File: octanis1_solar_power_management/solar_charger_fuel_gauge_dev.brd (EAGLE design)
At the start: 100 x 30 mm, 116 parts, among them IC1 REG1117, IC401 TUSB2046BIRHBIRHB, Q2 32.768kHz, Q4 CSTCR4M00G15L99, Q401 CSTCR6M00G15L99, T1 BC547, T2 BC547, U1 BQ24210, U2 BQ27510_DRZ_12, U3 DRV8836DSSR, U4 DRV8836DSSR, U402 TPS62237DRY, U404 TPD2E001DRLR, U5 DRV8836DSSR, U6 MSP430F5529IPNR, U7 DRV8836DSSR

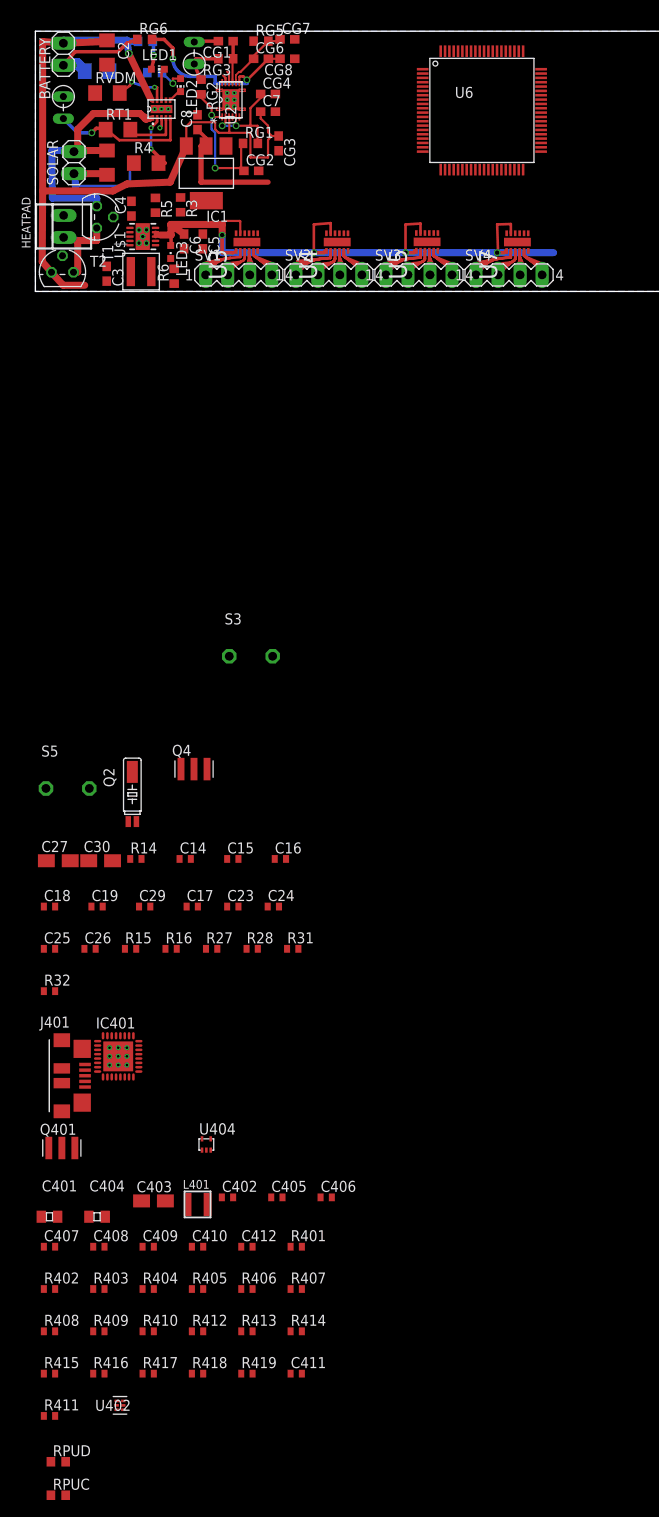
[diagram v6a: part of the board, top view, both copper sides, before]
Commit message: connected h-bridges to pins
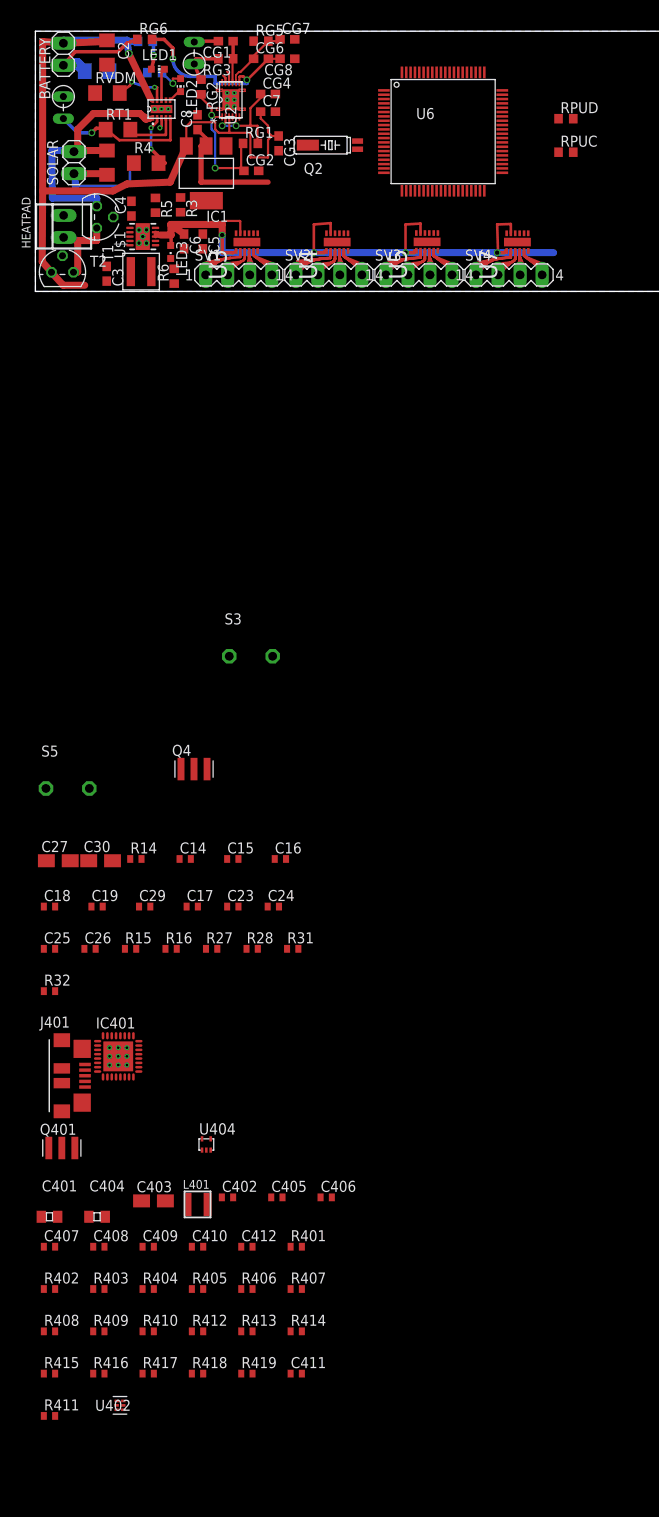
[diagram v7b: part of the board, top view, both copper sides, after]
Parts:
- moved RPUD 165.5 mm to (61.2, 19.9)
- moved RPUC 165.5 mm to (61.2, 16.1)
- moved Q2 76.6 mm to (32.7, 16.9), turned to 90 degrees
- moved U6 5.09 mm to (47.0, 18.4)

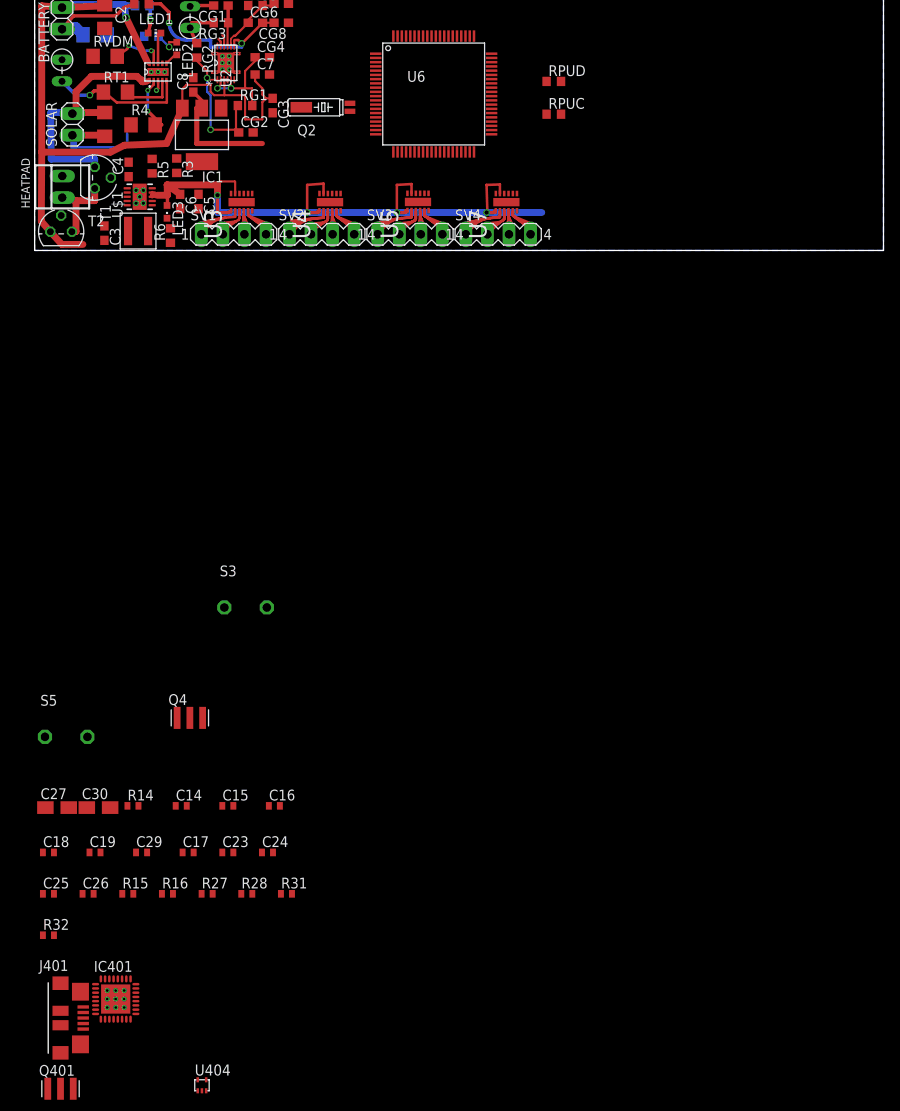
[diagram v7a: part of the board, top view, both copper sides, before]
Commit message: h-bridge: connected sleep pin with mode pin
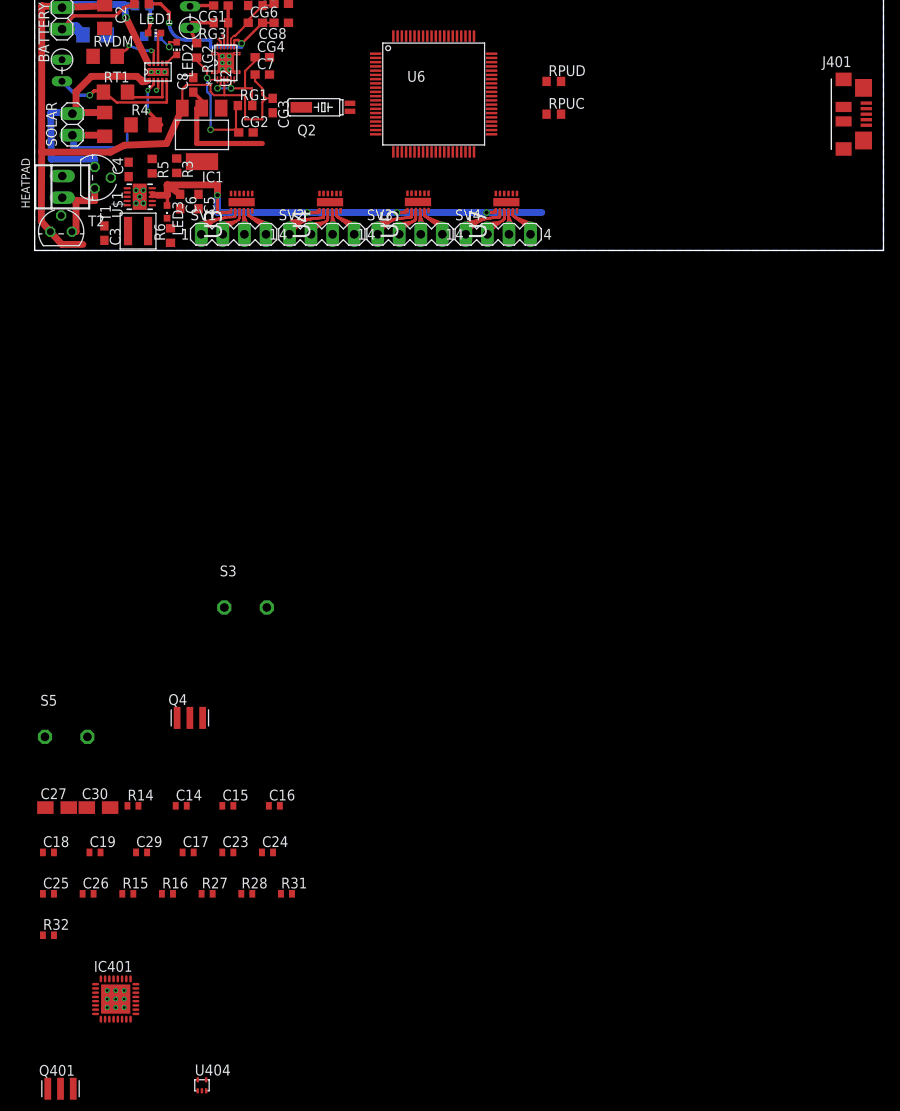
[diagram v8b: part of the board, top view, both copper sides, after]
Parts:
- moved J401 140.9 mm to (95.3, 16.1)
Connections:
- net +5V: no longer U3.11, U4.11, U5.11, U7.11
- net M12SLEEP: now also U3.11
- net M34SLEEP: now also U4.11
- net M56SLEEP: now also U5.11
- net M78SLEEP: now also U7.11
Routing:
- net +5V: track 84.1 -> 62.1 mm
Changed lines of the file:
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@@
 <attribute name="PACKAGE_DESIGNATOR" value="DRY" x="-3.8608" y="-84.328" size="1.778" layer="27" display="off"/>
 </element>
-<element name="J401" library="usb_con-update" package="HIROSE-ZX62R-B-5P" value="" x="3.048" y="-90.424"/>
+<element name="J401" library="usb_con-update" package="HIROSE-ZX62R-B-5P" value="" x="95.3008" y="16.0528"/>
 <element name="C404" library="CAP" package="CSMD0805" value="1u" x="7.112" y="-106.68"/>
 <element name="C401" library="CAP" package="CSMD0805" value="1u" x="1.6256" y="-106.68"/>
@@
 <wire x1="19.3444" y1="-124.7648" x2="25.034" y2="-124.7648" width="0" layer="19" extent="1-1"/>
 <wire x1="18.0444" y1="-119.888" x2="19.3444" y2="-124.7648" width="0" layer="19" extent="1-1"/>
-<wire x1="5.723" y1="-89.124" x2="3.048" y2="-98.7552" width="0" layer="19" extent="1-1"/>
-<wire x1="7.1754" y1="-89.4388" x2="5.723" y2="-89.124" width="0" layer="19" extent="1-1"/>
+<wire x1="97.9758" y1="17.3528" x2="3.048" y2="-98.7552" width="0" layer="19" extent="1-1"/>
+<wire x1="7.1754" y1="-89.4388" x2="97.9758" y2="17.3528" width="0" layer="19" extent="1-1"/>
 <wire x1="8.3004" y1="-85.8138" x2="7.1754" y2="-89.4388" width="0" layer="19" extent="1-1"/>
 <wire x1="9.8004" y1="-85.8138" x2="8.3004" y2="-85.8138" width="0" layer="19" extent="1-1"/>
@@
 <wire x1="21.5392" y1="6.5024" x2="21.5392" y2="4.4704" width="0.8128" layer="16"/>
 <wire x1="21.5392" y1="4.4704" x2="32.1056" y2="4.4704" width="0.8128" layer="16"/>
-<contactref element="U3" pad="11"/>
-<contactref element="U4" pad="11"/>
-<contactref element="U5" pad="11"/>
-<contactref element="U7" pad="11"/>
 <wire x1="32.1056" y1="4.4704" x2="42.672" y2="4.4704" width="0.8128" layer="16"/>
 <wire x1="42.672" y1="4.4704" x2="53.2384" y2="4.4704" width="0.8128" layer="16"/>
 <wire x1="53.2384" y1="4.4704" x2="59.7408" y2="4.4704" width="0.8128" layer="16"/>
-<wire x1="23.622" y1="6.7056" x2="23.622" y2="8.0772" width="0.254" layer="1"/>
-<wire x1="23.622" y1="8.0772" x2="23.5712" y2="8.128" width="0.254" layer="1"/>
-<wire x1="23.5712" y1="8.128" x2="21.9456" y2="8.128" width="0.254" layer="1"/>
-<wire x1="21.9456" y1="8.128" x2="21.5392" y2="7.7216" width="0.254" layer="1"/>
 <wire x1="23.1394" y1="4.6736" x2="22.8854" y2="4.4958" width="0.3048" layer="1"/>
 <wire x1="22.8854" y1="4.4958" x2="22.7584" y2="4.4704" width="0.4064" layer="1"/>
@@
 <wire x1="21.5392" y1="4.4704" x2="21.5392" y2="6.5024" width="0.4064" layer="1"/>
 <via x="32.1056" y="4.4704" extent="1-16" drill="0.5"/>
-<wire x1="34.036" y1="6.7056" x2="34.036" y2="7.874" width="0.3048" layer="1"/>
-<wire x1="34.036" y1="7.874" x2="32.1056" y2="7.7216" width="0.3048" layer="1"/>
-<wire x1="32.1056" y1="7.7216" x2="32.1056" y2="4.4704" width="0.3048" layer="1"/>
 <wire x1="43.9166" y1="4.699" x2="43.688" y2="4.699" width="0.3048" layer="1"/>
 <wire x1="43.688" y1="4.699" x2="43.688" y2="4.4704" width="0.3048" layer="1"/>
 <wire x1="43.688" y1="4.4704" x2="42.672" y2="4.4704" width="0.4064" layer="1"/>
 <via x="42.672" y="4.4704" extent="1-16" drill="0.5"/>
-<wire x1="44.3992" y1="6.731" x2="44.3992" y2="7.8232" width="0.3048" layer="1"/>
-<wire x1="44.3992" y1="7.8232" x2="42.672" y2="7.7216" width="0.3048" layer="1"/>
-<wire x1="42.672" y1="7.7216" x2="42.672" y2="4.4704" width="0.3048" layer="1"/>
 <wire x1="54.3306" y1="4.6736" x2="54.1528" y2="4.6736" width="0.3048" layer="1"/>
 <wire x1="54.1528" y1="4.6736" x2="54.1528" y2="4.4704" width="0.3048" layer="1"/>
-<wire x1="54.1528" y1="4.4704" x2="53.34" y2="4.4704" width="0.4064" layer="1"/>
+<wire x1="54.1528" y1="4.4704" x2="53.2384" y2="4.4704" width="0.4064" layer="1"/>
 <via x="53.2384" y="4.4704" extent="1-16" drill="0.5"/>
-<wire x1="53.34" y1="4.4704" x2="53.2384" y2="4.4704" width="0.4064" layer="1"/>
-<wire x1="54.8132" y1="6.7056" x2="54.8132" y2="7.7724" width="0.3048" layer="1"/>
-<wire x1="54.8132" y1="7.7724" x2="53.2384" y2="7.7216" width="0.3048" layer="1"/>
-<wire x1="53.2384" y1="7.7216" x2="53.34" y2="4.4704" width="0.3048" layer="1"/>
 <wire x1="33.5534" y1="4.6736" x2="33.3756" y2="4.6736" width="0.3048" layer="1"/>
 <wire x1="33.3756" y1="4.6736" x2="33.3756" y2="4.4704" width="0.3048" layer="1"/>
 <wire x1="33.3756" y1="4.4704" x2="32.1056" y2="4.4704" width="0.4064" layer="1"/>
-<wire x1="53.2384" y1="7.7216" x2="49.7578" y2="25.2552" width="0" layer="19" extent="1-1"/>
+<wire x1="54.1528" y1="4.6736" x2="49.7578" y2="25.2552" width="0" layer="19" extent="1-1"/>
 <wire x1="16.7386" y1="9.1322" x2="15.6092" y2="7.7216" width="0" layer="19" extent="1-1"/>
 <wire x1="19.304" y1="6.6158" x2="17.145" y2="6.6158" width="0" layer="19" extent="1-1"/>
@@
 <contactref element="J401" pad="SHIELD1"/>
 <contactref element="R401" pad="1"/>
-<wire x1="29.4236" y1="-110.1344" x2="3.048" y2="-86.324" width="0" layer="19" extent="1-1"/>
+<wire x1="29.4236" y1="-110.1344" x2="95.3008" y2="20.1528" width="0" layer="19" extent="1-1"/>
 </signal>
 <signal name="N$16">
@@
 <contactref element="R405" pad="2"/>
 <wire x1="19.2104" y1="-97.6988" x2="19.3444" y2="-115.0112" width="0" layer="19" extent="1-1"/>
-<wire x1="5.723" y1="-90.424" x2="19.2104" y2="-97.6988" width="0" layer="19" extent="1-1"/>
+<wire x1="97.9758" y1="16.0528" x2="19.2104" y2="-97.6988" width="0" layer="19" extent="1-1"/>
 </signal>
 <signal name="N$17">
@@
 <contactref element="R406" pad="2"/>
 <wire x1="20.2104" y1="-98.9988" x2="25.034" y2="-115.0112" width="0" layer="19" extent="1-1"/>
-<wire x1="5.723" y1="-91.074" x2="20.2104" y2="-98.9988" width="0" layer="19" extent="1-1"/>
+<wire x1="97.9758" y1="15.4028" x2="20.2104" y2="-98.9988" width="0" layer="19" extent="1-1"/>
 </signal>
 <signal name="N$18">
@@
 <wire x1="21.4988" y1="-104.4448" x2="14.9894" y2="-104.8512" width="0" layer="19" extent="1-1"/>
 <wire x1="19.2104" y1="-98.9988" x2="21.4988" y2="-104.4448" width="0" layer="19" extent="1-1"/>
-<wire x1="5.723" y1="-91.724" x2="8.0518" y2="-106.68" width="0" layer="19" extent="1-1"/>
+<wire x1="97.9758" y1="14.7528" x2="8.0518" y2="-106.68" width="0" layer="19" extent="1-1"/>
 </signal>
 <signal name="BAT-" class="4">
@@
 <signal name="M12SLEEP">
 <contactref element="U3" pad="12"/>
+<contactref element="U3" pad="11"/>
+<wire x1="23.622" y1="6.7056" x2="23.1394" y2="6.7056" width="0" layer="19" extent="1-1"/>
 </signal>
 <signal name="M1IN2">
@@
 <signal name="M34SLEEP">
 <contactref element="U4" pad="12"/>
+<contactref element="U4" pad="11"/>
+<wire x1="34.036" y1="6.7056" x2="33.5534" y2="6.7056" width="0" layer="19" extent="1-1"/>
 </signal>
 <signal name="M3IN1">
@@
 <signal name="M56SLEEP">
 <contactref element="U5" pad="12"/>
+<contactref element="U5" pad="11"/>
+<wire x1="44.3992" y1="6.731" x2="43.9166" y2="6.731" width="0" layer="19" extent="1-1"/>
 </signal>
 <signal name="M5IN1">
@@
 <signal name="M78SLEEP">
 <contactref element="U7" pad="12"/>
+<contactref element="U7" pad="11"/>
+<wire x1="54.8132" y1="6.7056" x2="54.3306" y2="6.7056" width="0" layer="19" extent="1-1"/>
 </signal>
 <signal name="M7IN1">
